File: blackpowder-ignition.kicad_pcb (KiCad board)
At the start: 2 copper layers, 63.5 x 63.5 mm, 43 parts, among them J1 CAS_stacking, J2 Conn_01x02, J3 Conn_01x02, J4 Conn_01x02, J5 Conn_01x02, J6 Conn_01x02, J7 Conn_01x02, J8 Conn_01x02, Q1 FDS6898A, Q2 FDS6898A, Q3 FDS6898A, Q4 FDS6898A, Q5 FDS6898A, Q6 FDS6898A, U1 TCA9555PWR

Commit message: removed circuits that can't be fit in
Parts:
- removed J6, J7: Conn_01x02, Connector_Molex:Molex_Mini-Fit_Jr_5569-02A2_2x01_P4.20mm_Horizontal
- removed Q5, Q6: FDS6898A, Package_SO:SOIC-8_3.9x4.9mm_P1.27mm
- removed R17, R19, R20, R21, R23, R24: R, Resistor_SMD:R_0603_1608Metric_Pad1.05x0.95mm_HandSolder
- removed R18, R22: R, star-common-lib:PWR163
- moved R10 1.21 mm to (82.3, 77.9)
- moved R6 1.02 mm to (72.1, 77.9)
- moved R14 0.95 mm to (93.2, 77.9)
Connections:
- U1 pad 13: /igniteE -> Net-(U1-Pad13)
- U1 pad 14: /~contE~ -> Net-(U1-Pad14)
- U1 pad 15: /igniteF -> Net-(U1-Pad15)
- U1 pad 16: /~igniteF~ -> Net-(U1-Pad16)
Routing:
- net /CAS_bus/I2C0_SDA: track 2.87 -> 0.00 mm
- net GND: track 174.6 -> 171.8 mm
- net Net-(J4-Pad2): track 15.3 -> 13.4 mm
- net Net-(J3-Pad2): track 15.4 -> 14.0 mm
- net +BATT: track 71.5 -> 72.9 mm
- net Net-(J5-Pad2): track 13.8 -> 12.5 mm
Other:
- net class BATT added: clearance 0.60452, trace_width 3.81, via_dia 0.8, via_drill 0.4

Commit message: everything hooked up, cleaned layout up, silkscreen
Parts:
- removed R10, R14, R2, R6: R, star-common-lib:PWR163
- added J10: Conn_01x03, star-common-lib:PWR163, F.Cu at (62.0, 77.5)
- added J6: Conn_01x03, star-common-lib:PWR163, F.Cu at (72.4, 77.5)
- added J7: Conn_01x03, star-common-lib:PWR163, F.Cu at (82.3, 77.5)
- added J9: Conn_01x03, star-common-lib:PWR163, F.Cu at (93.5, 77.5)
- moved R16 10.8 mm to (94.6, 93.5)
- moved R12 5.66 mm to (84.1, 94.9)
- moved R4 5.51 mm to (74.2, 98.4)
- moved R8 4.83 mm to (74.2, 96.6)
- moved JP1 0.13 mm to (66.0, 103.5)
- moved JP2 0.13 mm to (69.8, 103.5)
- moved JP3 0.13 mm to (73.9, 103.5)
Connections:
- net /CAS_bus/I2C0_SCL renamed /SCL
- net /CAS_bus/I2C0_SDA renamed /SDA
- net /CAS_bus/I2C1_SCL renamed Net-(J1-PadA17)
- net /CAS_bus/I2C1_SDA renamed Net-(J1-PadA18)
- net /CAS_bus/INT1 renamed Net-(J1-PadA1)
- net /CAS_bus/INT2 renamed Net-(J1-PadA2)
- net /CAS_bus/INT3 renamed Net-(J1-PadA9)
- net /CAS_bus/INT4 renamed Net-(J1-PadA10)
- net /CAS_bus/INT5 renamed Net-(J1-PadA11)
- net /CAS_bus/INT6 renamed Net-(J1-PadA12)
- net /CAS_bus/INT7 renamed Net-(J1-PadA19)
- net /CAS_bus/INT8 renamed Net-(J1-PadA20)
- net /CAS_bus/SPI0_MISO renamed Net-(J1-PadA27)
- net /CAS_bus/SPI0_MOSI renamed Net-(J1-PadA31)
- net /CAS_bus/SPI0_SCK renamed Net-(J1-PadA23)
- net /CAS_bus/SPI0_nSS1 renamed Net-(J1-PadA21)
- net /CAS_bus/SPI0_nSS2 renamed Net-(J1-PadA22)
- net /CAS_bus/SPI0_nSS3 renamed Net-(J1-PadA24)
- net /CAS_bus/SPI0_nSS4 renamed Net-(J1-PadA26)
- net /CAS_bus/SPI0_nSS5 renamed Net-(J1-PadA28)
- net /CAS_bus/SPI0_nSS6 renamed Net-(J1-PadA30)
- net /CAS_bus/SPI0_nSS7 renamed Net-(J1-PadA32)
- net /CAS_bus/SPI0_nSS8 renamed Net-(J1-PadA34)
- net /CAS_bus/SPIHS_MISO renamed Net-(J1-PadB6)
- net /CAS_bus/SPIHS_MOSI renamed Net-(J1-PadB9)
- net /CAS_bus/SPIHS_SCK renamed Net-(J1-PadB1)
- net /CAS_bus/SPIHS_nSS1 renamed Net-(J1-PadB13)
- net /CAS_bus/SPIHS_nSS2 renamed Net-(J1-PadB14)
- J1 pad A15: GND -> Net-(J1-PadA15)
- J1 pad A16: GND -> Net-(J1-PadA16)
- J1 pad A25: GND -> Net-(J1-PadA25)
- J1 pad A29: GND -> Net-(J1-PadA29)
- J1 pad A3: GND -> Net-(J1-PadA3)
- J1 pad A33: GND -> Net-(J1-PadA33)
- J1 pad A39: +BATT -> Net-(J1-PadA39)
- J1 pad A4: GND -> Net-(J1-PadA4)
- J1 pad A40: +BATT -> Net-(J1-PadA40)
- J1 pad A5: +5V -> Net-(J1-PadA5)
- J1 pad A6: +5V -> Net-(J1-PadA6)
- J1 pad A7: GND -> Net-(J1-PadA7)
- J1 pad A8: GND -> Net-(J1-PadA8)
- J1 pad B10: GND -> Net-(J1-PadB10)
- J1 pad B11: GND -> Net-(J1-PadB11)
- J1 pad B12: GND -> Net-(J1-PadB12)
- J1 pad B2: GND -> Net-(J1-PadB2)
- J1 pad B3: GND -> Net-(J1-PadB3)
- J1 pad B4: GND -> Net-(J1-PadB4)
- J1 pad B5: GND -> Net-(J1-PadB5)
- J1 pad B7: GND -> Net-(J1-PadB7)
- J1 pad B8: GND -> Net-(J1-PadB8)
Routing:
- net /~contD~: track 0.00 -> 52.5 mm, vias 1 -> 2
- net /igniteD: track 3.89 -> 53.8 mm, vias 1 -> 2
- net /~contC~: track 0.00 -> 43.3 mm, vias 1 -> 2
- net /~contA~: track 0.62 -> 43.8 mm, vias 0 -> 2
- net /igniteC: track 4.00 -> 44.8 mm, vias 1 -> 2
- net /SCL: track 0.53 -> 38.1 mm
- net /SDA: track 0.00 -> 36.1 mm
- net /~contB~: track 0.00 -> 36.0 mm, vias 0 -> 2
- net /igniteB: track 4.27 -> 36.6 mm, vias 1 -> 2
- net /igniteA: track 4.37 -> 34.1 mm, vias 1 -> 2
- net GND: track 171.8 -> 146.7 mm, vias 0 -> 18
- net +3V3: track 50.8 -> 63.0 mm
- added copper zone on F.Cu, net +BATT
- added copper zone on F.Cu, net GND
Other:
- board text added: "A"
- board text added: "B"
- board text added: "BATTERY"
- board text added: "C"
- board text added: "D"

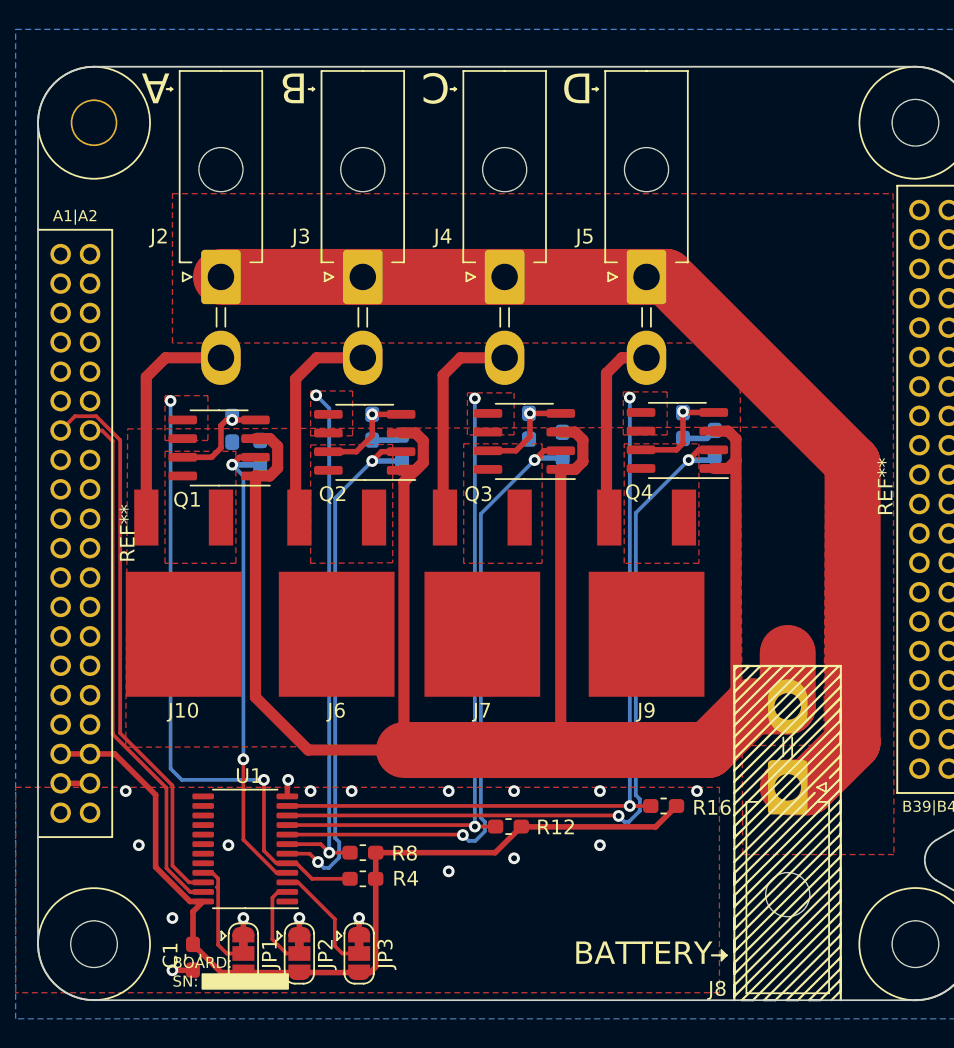
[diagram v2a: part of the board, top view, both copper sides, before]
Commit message: pours for high current traces to connectors
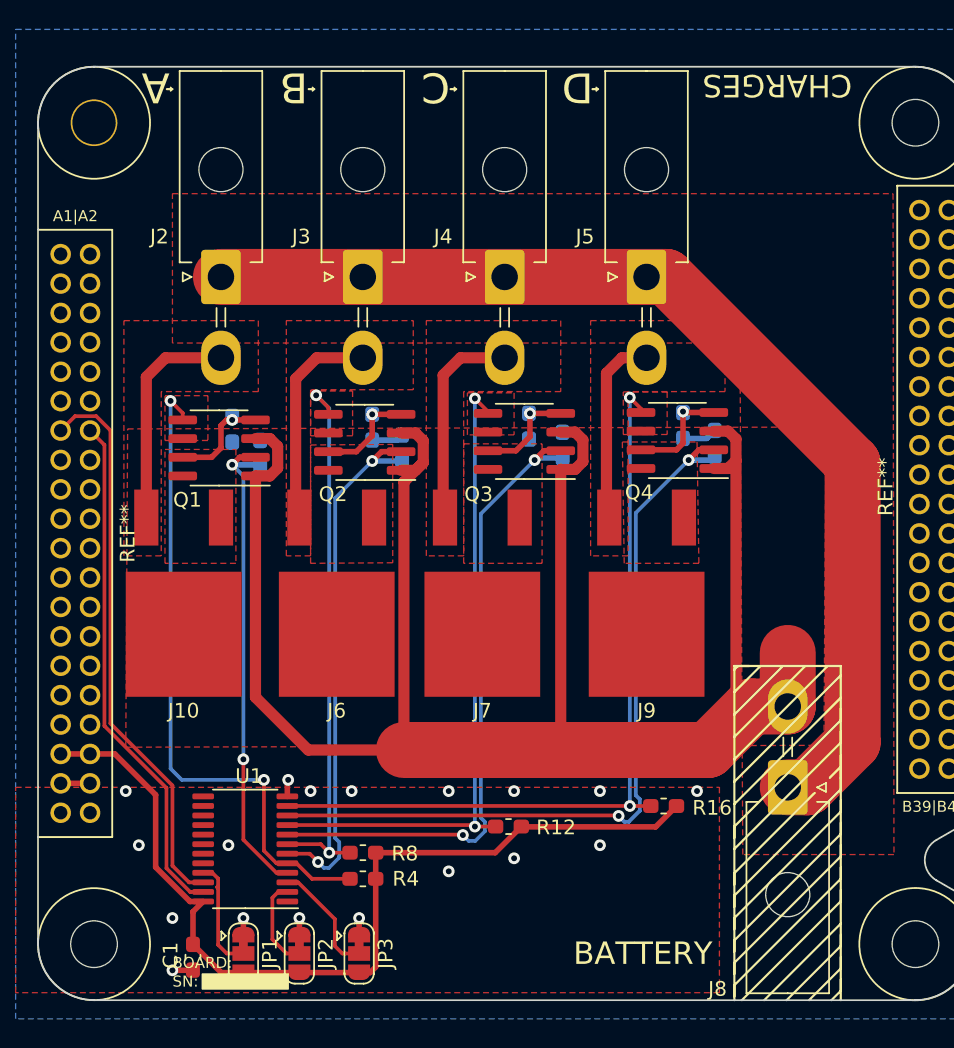
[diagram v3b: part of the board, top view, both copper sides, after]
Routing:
- net /~contB~: track 36.0 -> 37.6 mm
- net /~contA~: track 43.8 -> 45.4 mm
- net /~contC~: track 43.3 -> 44.7 mm
- net /~contD~: track 52.5 -> 53.8 mm
- added copper zone on F.Cu, net Net-(J10-Pad1)
- added copper zone on F.Cu, net Net-(J3-Pad2)
- added copper zone on F.Cu, net Net-(J4-Pad2)
- added copper zone on F.Cu, net Net-(J5-Pad2)
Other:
- board text added: "CHARGES"

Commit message: most functionality
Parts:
- removed J10, J6, J7, J9: Conn_01x03, star-common-lib:PWR163
- added R10: 3R, star-common-lib:PWR163, F.Cu at (93.5, 78.0)
- added R14: 3R, star-common-lib:PWR163, F.Cu at (61.7, 78.0)
- added R2: 3R, star-common-lib:PWR163, F.Cu at (72.2, 78.0)
- added R6: 3R, star-common-lib:PWR163, F.Cu at (82.4, 78.0)
- added TP1: TestPoint, star-common-lib:TestPoint_Keystone_5117_Miniature, F.Cu at (80.0, 100.8)
- added TP10: TestPoint, star-common-lib:TestPoint_Keystone_5000_Miniature, F.Cu at (103.0, 81.1)
- added TP11: TestPoint, star-common-lib:TestPoint_Keystone_5000_Miniature, F.Cu at (58.2, 97.2)
- added TP2: TestPoint, star-common-lib:TestPoint_Keystone_5117_Miniature, F.Cu at (83.8, 100.8)
- added TP3: TestPoint, star-common-lib:TestPoint_Keystone_5117_Miniature, F.Cu at (87.5, 100.8)
- added TP4: TestPoint, star-common-lib:TestPoint_Keystone_5117_Miniature, F.Cu at (91.2, 100.8)
- added TP5: TestPoint, star-common-lib:TestPoint_Keystone_5117_Miniature, F.Cu at (82.0, 104.2)
- added TP6: TestPoint, star-common-lib:TestPoint_Keystone_5117_Miniature, F.Cu at (85.8, 104.2)
- added TP7: TestPoint, star-common-lib:TestPoint_Keystone_5117_Miniature, F.Cu at (89.5, 104.2)
- added TP8: TestPoint, star-common-lib:TestPoint_Keystone_5117_Miniature, F.Cu at (93.2, 104.2)
- added TP9: TestPoint, star-common-lib:TestPoint_Keystone_5000_Miniature, F.Cu at (108.5, 92.5)
- J2, J3, J4, J5, J8: footprint Connector_Molex:Molex_Mini-Fit_Jr_5569-02A2_2x01_P4.20mm_Horizontal -> star-common-lib:Molex_Mini-Fit_Jr_5569-02A2_2x01_P4.20mm_Horizontal
- R1, R11, R13, R15, R3, R5, R7, R9: value R -> 100k
- R12, R16, R4, R8: value R -> 50k
- U1: value TCA9555PWR -> TCA9534; footprint Package_SO:TSSOP-24_4.4x7.8mm_P0.65mm -> Package_SO:TSSOP-16_4.4x5mm_P0.65mm
- moved C1 9.81 mm to (60.8, 94.1)
- moved R8 8.84 mm to (83.0, 97.0)
- moved R4 5.28 mm to (79.2, 97.0)
- moved R16 5.24 mm to (90.8, 97.0)
- moved JP1 3.50 mm to (62.5, 103.5)
- moved JP2 3.50 mm to (66.3, 103.5)
- moved JP3 3.50 mm to (70.4, 103.5)
- moved R12 3.42 mm to (86.8, 97.0)
- moved R13 3.14 mm to (95.0, 69.2), turned to 180 degrees
- moved R9 3.02 mm to (84.8, 69.2), turned to 180 degrees
- moved R1 2.82 mm to (64.4, 69.8), turned to 180 degrees
- moved R5 2.74 mm to (74.1, 69.5), turned to 180 degrees
- moved U1 1.42 mm to (64.8, 96.2), turned to 90 degrees
- moved R15 1.27 mm to (95.0, 66.8), turned to 180 degrees
- moved R11 1.14 mm to (84.8, 66.8), turned to 180 degrees
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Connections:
- Q1 pad 3: GND -> /~contA~
- Q1 pad 5: /~contA~ -> +3V3
- Q1 pad 6: /~contA~ -> +3V3
- Q2 pad 3: GND -> /~contB~
- Q2 pad 5: /~contB~ -> +3V3
- Q2 pad 6: /~contB~ -> +3V3
- Q3 pad 3: GND -> /~contC~
- Q3 pad 5: /~contC~ -> +3V3
- Q3 pad 6: /~contC~ -> +3V3
- Q4 pad 3: GND -> /~contD~
- Q4 pad 5: /~contD~ -> +3V3
- Q4 pad 6: /~contD~ -> +3V3
- R12 pad 1: +3V3 -> /~contC~
- R12 pad 2: /~contC~ -> GND
- R16 pad 1: +3V3 -> /~contD~
- R16 pad 2: /~contD~ -> GND
- R4 pad 1: +3V3 -> /~contA~
- R4 pad 2: /~contA~ -> GND
- R8 pad 1: +3V3 -> /~contB~
- R8 pad 2: /~contB~ -> GND
- U1 pad 1: Net-(U1-Pad1) -> /A0
- U1 pad 10: /igniteD -> /~contC~
- U1 pad 11: /~contD~ -> /igniteD
- U1 pad 12: GND -> /~contD~
- U1 pad 14: Net-(U1-Pad14) -> /SCL
- U1 pad 15: Net-(U1-Pad15) -> /SDA
- U1 pad 16: Net-(U1-Pad16) -> +3V3
- U1 pad 8: /igniteC -> GND
- U1 pad 9: /~contC~ -> /igniteC
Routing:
- net +3V3: track 63.0 -> 98.0 mm, vias 0 -> 4
- net /~contB~: track 37.6 -> 63.7 mm
- net /igniteB: track 36.6 -> 59.0 mm
- net /~contD~: track 53.8 -> 73.8 mm
- net GND: track 146.7 -> 127.5 mm, vias 18 -> 9
- net /igniteD: track 53.8 -> 72.0 mm
- net /~contC~: track 44.7 -> 61.3 mm, vias 2 -> 3
- net /igniteA: track 34.1 -> 50.3 mm
- net /~contA~: track 45.4 -> 59.0 mm
- net /igniteC: track 44.8 -> 53.1 mm, vias 2 -> 3
- net +BATT: track 72.9 -> 78.1 mm
- net /SCL: track 38.1 -> 34.1 mm
- net /SDA: track 35.6 -> 32.0 mm
- net /A0: track 7.57 -> 5.62 mm
- net Net-(Q4-Pad4): track 7.32 -> 6.12 mm
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- added copper zone on F.Cu, net +3V3
- removed copper zone on F.Cu, net +BATT
- removed copper zone on F.Cu, net /~contA~
- removed copper zone on F.Cu, net /~contB~
- removed copper zone on F.Cu, net /~contC~
- removed copper zone on F.Cu, net /~contD~
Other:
- net class Default: clearance 0.1524 -> 0.254; trace_width 0.2032 -> 0.254
- rule trace_clearance: 0.1524 -> 0.254
- board text added: "+3.3V"
- board text added: "+BATT"
- board text added: "0"
- board text added: "1"
- board text added: "A0"
- board text added: "A1"
- board text added: "A2"
- board text added: "BATT"
- board text added: "HIGH PWR GND"
- board text added: "ignite"
- board text added: "~cont~"
- board text removed: "BATTERY"

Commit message: updated submodules to master
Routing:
- net GND: vias 9 -> 10
